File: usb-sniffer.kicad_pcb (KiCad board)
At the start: 2 copper layers, 23 parts, among them J1 USB_C_Receptacle_USB2.0_16P, U1 CY7C68013A-56PVX, U2 24LC128, Y1 24MHz

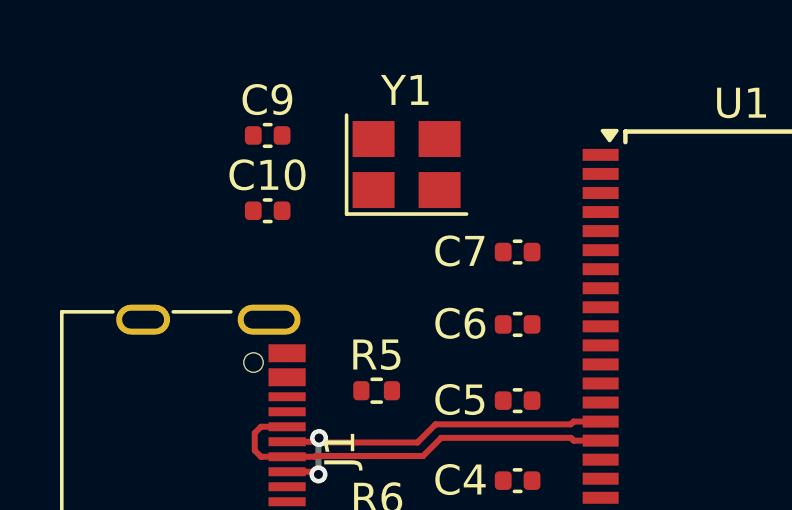
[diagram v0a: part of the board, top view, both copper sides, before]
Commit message: modified .gitignore
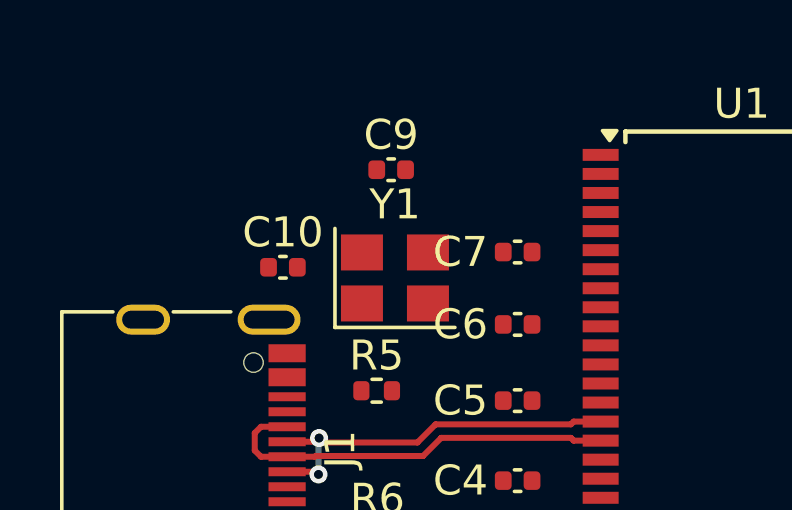
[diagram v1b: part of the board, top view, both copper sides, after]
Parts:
- moved C9 4.27 mm to (126.3, 83.3)
- moved Y1 3.80 mm to (126.4, 86.9)
- moved C10 1.95 mm to (122.7, 86.6)
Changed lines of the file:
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@@
 	(footprint "Capacitor_SMD:C_0402_1005Metric"
 		(layer "F.Cu")
-		(at 122.1486 82.169)
+		(at 126.2634 83.312)
 		(descr "Capacitor SMD 0402 (1005 Metric), square (rectangular) end terminal, IPC_7351 nominal, (Body size source: IPC-SM-782 page 76, https://www.pcb-3d.com/wordpress/wp-content/uploads/ipc-sm-782a_amendment_1_and_2.pdf), generated with kicad-footprint-generator")
 		(tags "capacitor")
@@
 	(footprint "Capacitor_SMD:C_0402_1005Metric"
 		(layer "F.Cu")
-		(at 122.1486 84.679)
+		(at 122.6566 86.5632)
 		(descr "Capacitor SMD 0402 (1005 Metric), square (rectangular) end terminal, IPC_7351 nominal, (Body size source: IPC-SM-782 page 76, https://www.pcb-3d.com/wordpress/wp-content/uploads/ipc-sm-782a_amendment_1_and_2.pdf), generated with kicad-footprint-generator")
 		(tags "capacitor")
@@
 	(footprint "Crystal:Crystal_SMD_3225-4Pin_3.2x2.5mm"
 		(layer "F.Cu")
-		(at 126.7786 83.139)
+		(at 126.3904 86.9188)
 		(descr "SMD Crystal SERIES SMD3225/4 http://www.txccrystal.com/images/pdf/7m-accuracy.pdf, 3.2x2.5mm^2 package")
 		(tags "SMD SMT crystal")

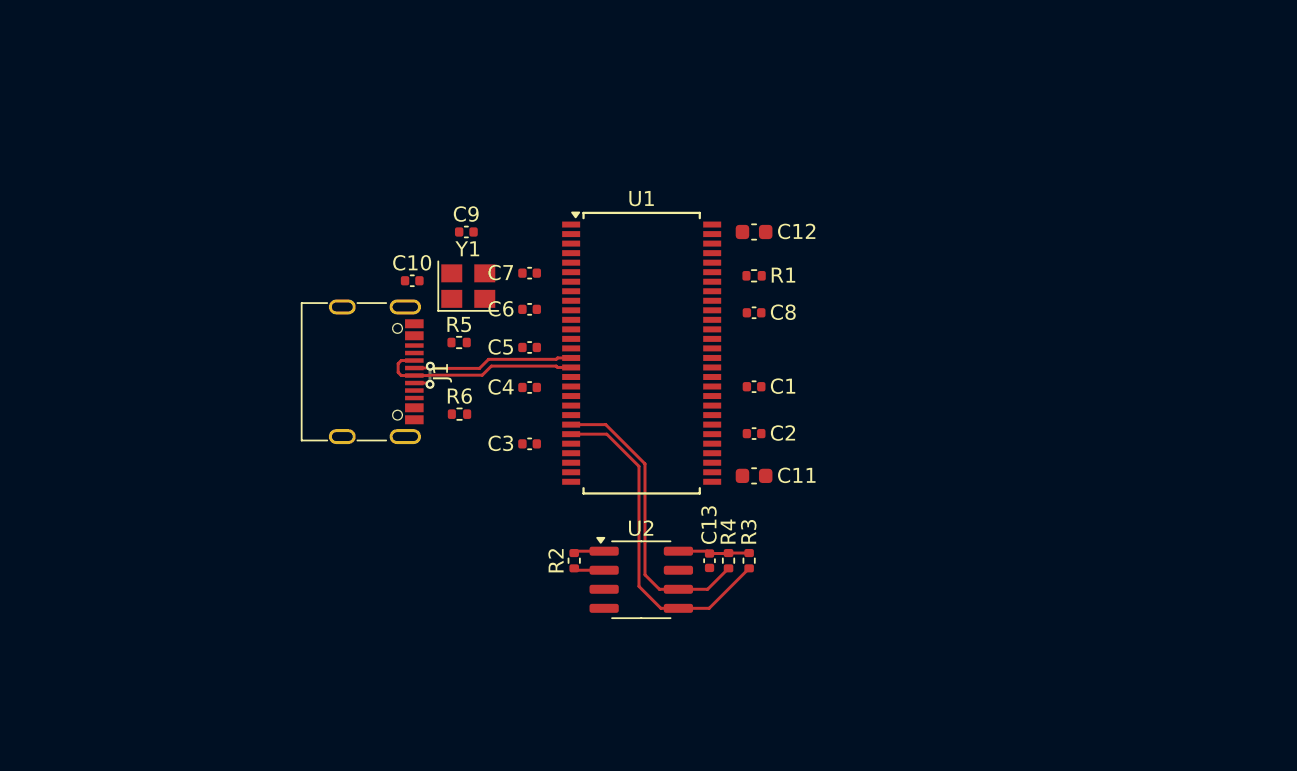
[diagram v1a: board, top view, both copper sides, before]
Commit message: Add USB3343
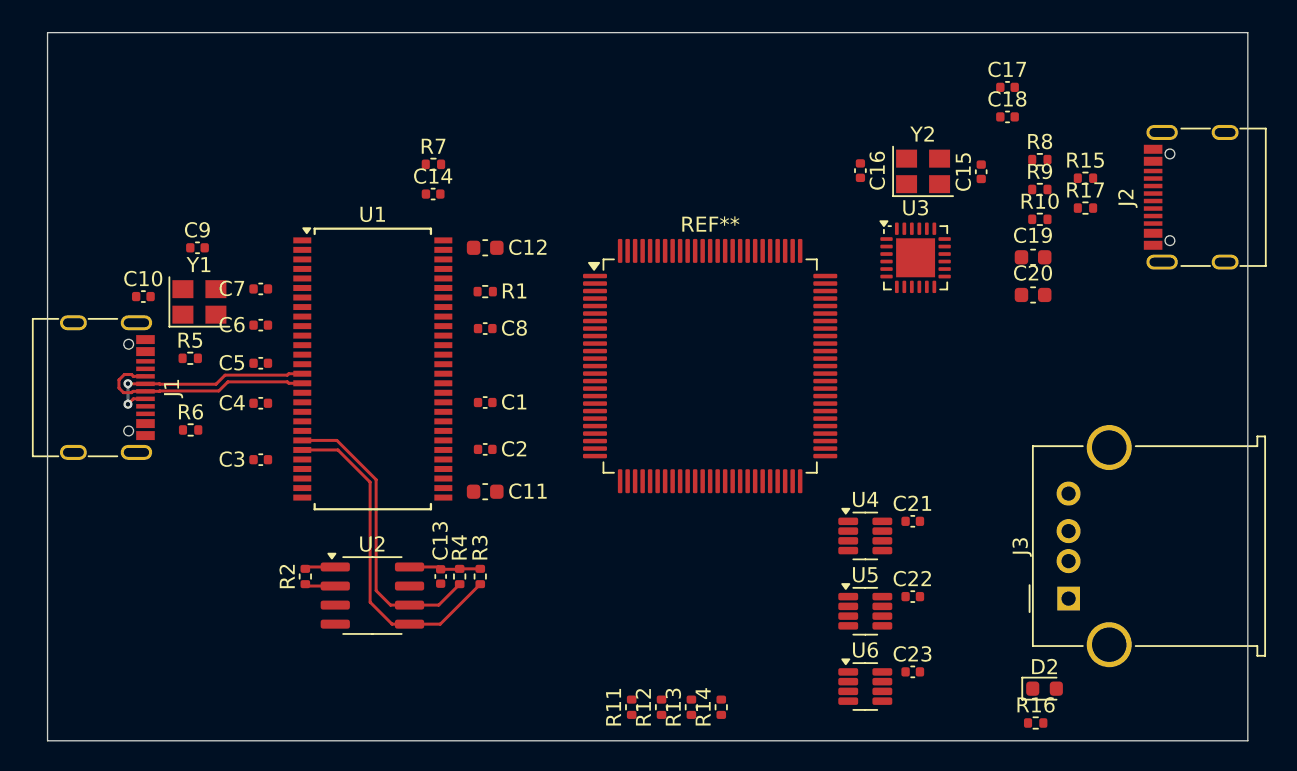
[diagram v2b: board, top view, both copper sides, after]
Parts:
- added C14: 100nF, Capacitor_SMD:C_0402_1005Metric, F.Cu at (124.0, 80.8)
- added C15: 22p, Capacitor_SMD:C_0402_1005Metric, F.Cu at (160.6, 79.3)
- added C16: 22p, Capacitor_SMD:C_0402_1005Metric, F.Cu at (152.5, 79.2)
- added C17: 100nF, Capacitor_SMD:C_0402_1005Metric, F.Cu at (162.3, 73.7)
- added C18: 100nF, Capacitor_SMD:C_0402_1005Metric, F.Cu at (162.3, 75.6)
- added C19: 2.2uF, Capacitor_SMD:C_0603_1608Metric, F.Cu at (164.0, 85.0)
- added C20: 2.2uF, Capacitor_SMD:C_0603_1608Metric, F.Cu at (164.0, 87.5)
- added C21: 100nF, Capacitor_SMD:C_0402_1005Metric, F.Cu at (156.0, 102.6)
- added C22: 100nF, Capacitor_SMD:C_0402_1005Metric, F.Cu at (156.0, 107.6)
- added C23: 100nF, Capacitor_SMD:C_0402_1005Metric, F.Cu at (156.0, 112.6)
- added D2: LED, LED_SMD:LED_0603_1608Metric, F.Cu at (164.8, 113.7)
- added J2: USB_C_Receptacle_USB2.0_16P, Connector_USB:USB_C_Receptacle_G-Switch_GT-USB-7010ASV, F.Cu at (175.8, 81.0)
- added J3: USB_A, Connector_USB:USB_A_Molex_67643_Horizontal, F.Cu at (166.4, 107.7)
- added R10: 8.06K, Resistor_SMD:R_0402_1005Metric, F.Cu at (164.5, 82.5)
- added R11: 10K, Resistor_SMD:R_0402_1005Metric, F.Cu at (137.3, 115.0)
- added R12: 33K, Resistor_SMD:R_0402_1005Metric, F.Cu at (139.3, 115.0)
- added R13: 4.7K, Resistor_SMD:R_0402_1005Metric, F.Cu at (141.3, 115.0)
- added R14: 4.7K, Resistor_SMD:R_0402_1005Metric, F.Cu at (143.3, 115.0)
- added R15: 5K1, Resistor_SMD:R_0402_1005Metric, F.Cu at (167.5, 79.7)
- added R16: 10K, Resistor_SMD:R_0402_1005Metric, F.Cu at (164.2, 116.0)
- added R17: 5K1, Resistor_SMD:R_0402_1005Metric, F.Cu at (167.5, 81.7)
- added R7: 10K, Resistor_SMD:R_0402_1005Metric, F.Cu at (124.1, 78.8)
- added R8: 10K, Resistor_SMD:R_0402_1005Metric, F.Cu at (164.5, 78.5)
- added R9: 20K, Resistor_SMD:R_0402_1005Metric, F.Cu at (164.5, 80.5)
- added REF**: LQFP-100_14x14mm_P0.5mm, Package_QFP:LQFP-100_14x14mm_P0.5mm, F.Cu at (142.5, 92.2)
- added U3: USB3343, Package_DFN_QFN:QFN-24-1EP_4x4mm_P0.5mm_EP2.6x2.6mm, F.Cu at (156.2, 85.0)
- added U4: MAX9032, Package_TO_SOT_SMD:SOT-23-8, F.Cu at (152.9, 103.6)
- added U5: MAX9032, Package_TO_SOT_SMD:SOT-23-8, F.Cu at (152.9, 108.6)
- added U6: MAX9032, Package_TO_SOT_SMD:SOT-23-8, F.Cu at (152.9, 113.6)
- added Y2: 26MHz, Crystal:Crystal_SMD_3225-4Pin_3.2x2.5mm, F.Cu at (156.7, 79.3)
- moved C1 18.0 mm to (127.5, 94.7)
- moved C11 18.0 mm to (127.5, 100.6)
- moved C12 18.0 mm to (127.5, 84.4)
- moved C13 18.0 mm to (124.6, 106.3)
- moved C2 18.0 mm to (127.5, 97.8)
- moved C3 18.0 mm to (112.6, 98.5)
- moved C4 18.0 mm to (112.6, 94.7)
- moved C5 18.0 mm to (112.6, 92.1)
- moved C6 18.0 mm to (112.6, 89.5)
- moved C7 18.0 mm to (112.6, 87.1)
- moved C8 18.0 mm to (127.5, 89.8)
- moved R1 18.0 mm to (127.5, 87.3)
- moved R2 18.0 mm to (115.5, 106.3)
- moved C10 18.0 mm to (104.7, 87.6)
- moved C9 18.0 mm to (108.3, 84.4)
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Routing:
- net /Host USB/D-: track 13.7 -> 15.2 mm
- net /Host USB/D+: track 13.2 -> 14.6 mm
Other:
- board outline added: 80 x 47.2 mm

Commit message: layout uncompleted
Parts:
- removed REF**: LQFP-100_14x14mm_P0.5mm, Package_QFP:LQFP-100_14x14mm_P0.5mm
- added C24: 100nF, Capacitor_SMD:C_0402_1005Metric, F.Cu at (131.9, 82.6)
- added C25: 100nF, Capacitor_SMD:C_0402_1005Metric, F.Cu at (150.5, 85.5)
- added C26: 100nF, Capacitor_SMD:C_0402_1005Metric, F.Cu at (150.7, 91.1)
- added C27: 100nF, Capacitor_SMD:C_0402_1005Metric, F.Cu at (150.9, 94.3)
- added C28: 100nF, Capacitor_SMD:C_0402_1005Metric, F.Cu at (130.3, 95.4)
- added C29: 100nF, Capacitor_SMD:C_0402_1005Metric, F.Cu at (132.4, 98.5)
- added C30: 100nF, Capacitor_SMD:C_0402_1005Metric, F.Cu at (146.4, 100.1)
- added C31: 100nF, Capacitor_SMD:C_0402_1005Metric, F.Cu at (142.7, 100.1)
- added D1: LED, LED_SMD:LED_0603_1608Metric, F.Cu at (140.0, 76.9)
- added D3: LED, LED_SMD:LED_0603_1608Metric, F.Cu at (142.5, 76.9)
- added D4: LED, LED_SMD:LED_0603_1608Metric, F.Cu at (145.1, 76.9)
- added D5: LED, LED_SMD:LED_0603_1608Metric, F.Cu at (147.7, 76.9)
- added R18: 10K, Resistor_SMD:R_0402_1005Metric, F.Cu at (130.0, 97.1)
- added R19: 2K2, Resistor_SMD:R_0402_1005Metric, F.Cu at (140.0, 74.1)
- added R20: 2K2, Resistor_SMD:R_0402_1005Metric, F.Cu at (142.5, 74.1)
- added R21: 2K2, Resistor_SMD:R_0402_1005Metric, F.Cu at (145.1, 74.1)
- added R22: 2K2, Resistor_SMD:R_0402_1005Metric, F.Cu at (147.7, 74.1)
- added TP1: Test, TestPoint:TestPoint_Pad_D1.0mm, B.Cu at (146.2, 87.2)
- added TP10: Test, TestPoint:TestPoint_Pad_D1.0mm, B.Cu at (104.4, 104.1)
- added TP11: Test, TestPoint:TestPoint_Pad_D1.0mm, B.Cu at (104.4, 107.1)
- added TP12: Test, TestPoint:TestPoint_Pad_D1.0mm, B.Cu at (104.4, 110.2)
- added TP2: Test, TestPoint:TestPoint_Pad_D1.0mm, B.Cu at (146.2, 90.2)
- added TP3: Test, TestPoint:TestPoint_Pad_D1.0mm, B.Cu at (143.2, 87.2)
- added TP4: Test, TestPoint:TestPoint_Pad_D1.0mm, B.Cu at (143.2, 90.2)
- added TP5: Test, TestPoint:TestPoint_Pad_D1.0mm, B.Cu at (140.1, 87.2)
- added TP6: Test, TestPoint:TestPoint_Pad_D1.0mm, B.Cu at (140.1, 90.2)
- added TP7: Test, TestPoint:TestPoint_Pad_D1.0mm, B.Cu at (137.1, 87.2)
- added TP8: Test, TestPoint:TestPoint_Pad_D1.0mm, B.Cu at (137.1, 90.2)
- added TP9: Test, TestPoint:TestPoint_Pad_D1.0mm, B.Cu at (104.4, 101.0)
- added U7: LCMXO2-2000HC-5TG100I, Package_QFP:LQFP-100_14x14mm_P0.5mm, F.Cu at (140.4, 90.3)
- moved C17 19.2 mm to (154.1, 91.1), turned to 180 degrees
- moved C13 18.0 mm to (107.9, 99.4), turned to 0 degrees
- moved R11 15.7 mm to (152.9, 113.1), turned to 180 degrees
- moved C12 15.3 mm to (113.0, 79.6)
- moved C14 15.2 mm to (108.9, 79.1)
- moved R7 15.2 mm to (109.0, 77.1)
- moved R3 15.1 mm to (113.5, 99.9), turned to 180 degrees
- moved R4 13.4 mm to (113.5, 100.9), turned to 180 degrees
- moved R14 12.7 mm to (150.0, 104.2), turned to -90 degrees
- moved C19 12.5 mm to (151.8, 82.3), turned to 90 degrees
- moved C18 12.3 mm to (160.8, 87.8)
- moved R8 12.0 mm to (153.1, 82.3), turned to -90 degrees
- moved R13 11.8 mm to (150.0, 107.0)
- moved U2 11.5 mm to (109.2, 103.6), turned to 90 degrees
- moved R12 11.5 mm to (149.9, 110.8)
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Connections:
- net /T_USB_DM renamed /T_USB_DN
- net Net-(U2-A1) renamed /Host USB/A1
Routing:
- net /T_USB_DN: track 0.00 -> 50.9 mm
- net /T_USB_DP: track 0.00 -> 49.5 mm
- net /FD3: track 0.00 -> 33.6 mm
- net /FD2: track 0.00 -> 33.0 mm
- net /FD1: track 0.00 -> 30.4 mm
- net /FD0: track 0.00 -> 29.8 mm
- net /IFCLK: track 0.00 -> 29.8 mm
- net +3V3: track 6.84 -> 36.5 mm
- net /FD13: track 0.00 -> 26.9 mm
- net /FD14: track 0.00 -> 26.0 mm
- net /SLRD: track 0.00 -> 25.6 mm
- net /FD15: track 0.00 -> 25.1 mm
- net /SLWR: track 0.00 -> 25.0 mm
- net /FD4: track 0.00 -> 17.3 mm
- net /FD5: track 0.00 -> 16.6 mm
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- added copper zone on In1.Cu, net GND
- added copper zone on In2.Cu, net GND
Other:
- board size 80 x 47.2 mm -> 80 x 47.4 mm
- copper layers 2 -> 4

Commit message: add side ground
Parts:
- added D6: BAT54S, Package_TO_SOT_SMD:SOT-23, F.Cu at (108.9, 78.2)
- added J4: Conn_01x02, Connector_PinHeader_2.54mm:PinHeader_1x02_P2.54mm_Vertical, F.Cu at (104.2, 78.1)
- moved C27 21.0 mm to (136.5, 78.9), turned to 90 degrees
- moved R16 10.2 mm to (154.7, 112.2)
- moved C29 9.82 mm to (130.2, 88.9)
- moved R7 8.48 mm to (117.4, 76.3)
- moved C12 8.48 mm to (121.4, 78.7)
- moved C14 8.48 mm to (117.4, 78.3)
- moved D2 7.02 mm to (158.0, 112.2)
- moved C22 5.57 mm to (160.8, 103.4)
- moved R11 5.57 mm to (157.8, 110.4)
- moved C21 5.57 mm to (160.8, 100.0)
- moved C23 5.57 mm to (160.8, 106.8)
- moved R13 5.57 mm to (154.9, 104.3)
- moved U4 5.57 mm to (157.8, 100.9)
- moved U5 5.57 mm to (157.8, 104.4)
- moved U6 5.57 mm to (157.8, 107.8)
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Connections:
- U7 pad 41: unconnected-(U7-PB18B-Pad41) -> /IO_IN
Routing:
- net +3V3: track 36.5 -> 47.3 mm
- net /DBG_0: track 0.00 -> 6.44 mm
- net /DBG_3: track 0.00 -> 6.20 mm
- net /DBG_1: track 0.00 -> 5.57 mm
- net /DBG_2: track 0.00 -> 5.33 mm
- net /Host USB/D+: track 26.1 -> 22.0 mm
- net /Host USB/D-: track 26.1 -> 23.5 mm
- net GND: vias 0 -> 80
- added copper zone on B.Cu, net GND
- added copper zone on F.Cu, net GND
